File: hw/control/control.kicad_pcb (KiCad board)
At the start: 2 copper layers, 160 x 90 mm, 144 parts, among them J101 Screw_Terminal_01x02, J102 Screw_Terminal_01x03, J103 Screw_Terminal_01x03, J301 Conn_02x05_Odd_Even, J302 Conn_01x04, J303 Raspberry_Pi_0_2_3, J304 Micro_SD_Card, J305 Conn_01x06, J306 Conn_01x07, Q1001 BC807, Q1002 BC817, Q401 BC817, Q501 BC817, Q601 BC817, Q701 BC817, Q801 BC807, Q802 BC817, Q901 AOSP21357, Q902 IRF4905, U1001 LM2678T-ADJ, U1101 SN74AHCT125D, U201 LM2596T-ADJ, U801 LM2678T-ADJ

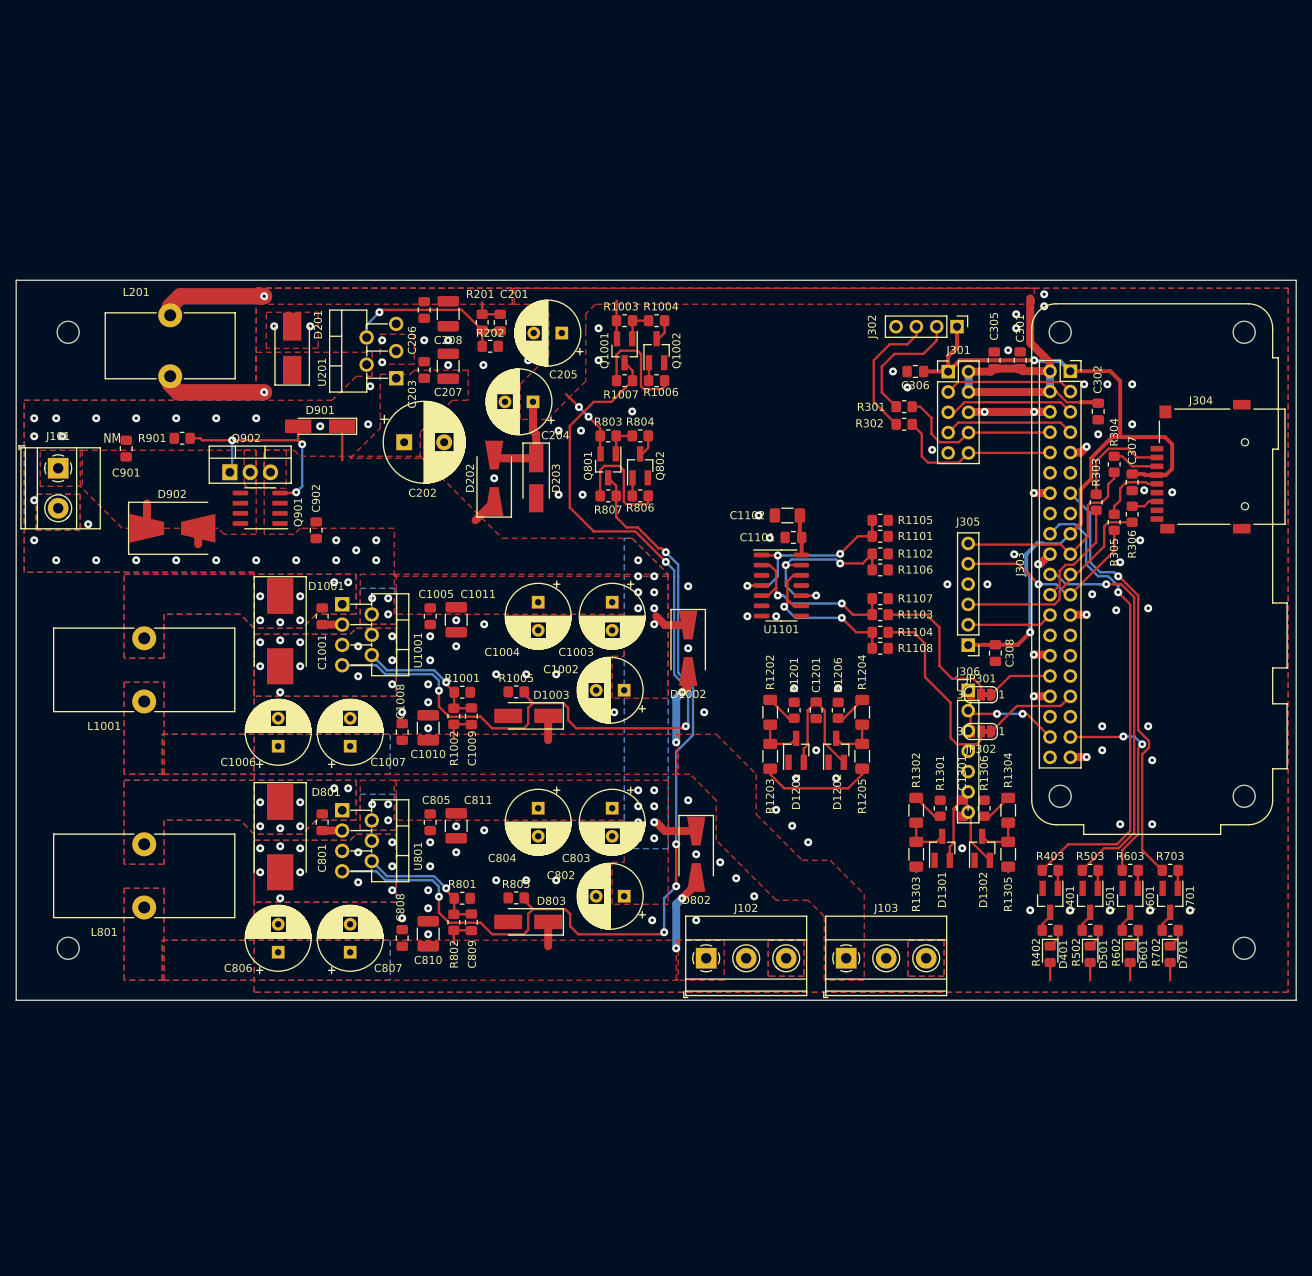
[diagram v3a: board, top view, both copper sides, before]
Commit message: [hw] Lay-out IIS module connector, pwr. enable
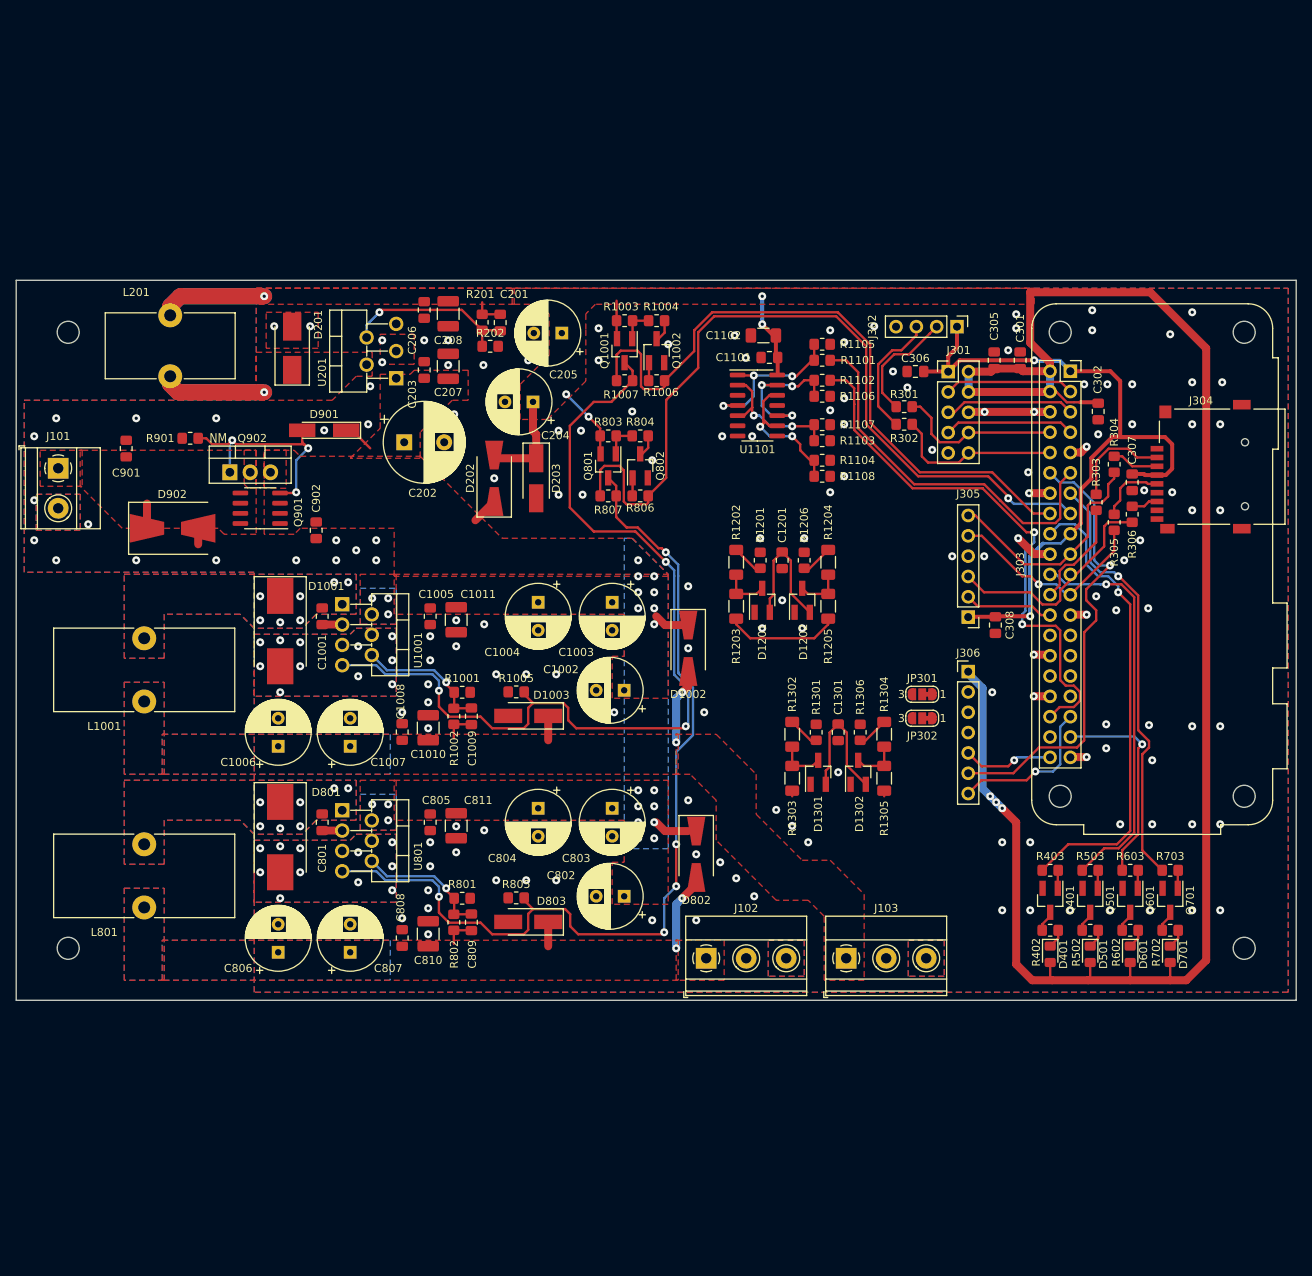
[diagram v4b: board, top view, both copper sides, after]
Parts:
- moved R1101 23.2 mm to (160.8, 60.0)
- moved R1105 23.2 mm to (160.8, 58.0)
- moved R1103 22.9 mm to (160.8, 70.0)
- moved R1107 22.9 mm to (160.8, 68.0)
- moved R1102 22.9 mm to (160.8, 62.5)
- moved R1106 22.9 mm to (160.8, 64.5)
- moved C1101 22.7 mm to (154.2, 59.6)
- moved C1102 22.7 mm to (153.4, 56.9)
- moved U1101 22.7 mm to (152.7, 65.7)
- moved R1104 22.7 mm to (160.8, 72.5)
- moved R1108 22.7 mm to (160.8, 74.5)
- moved C1201 19.2 mm to (155.8, 85.0)
- moved D1201 19.2 mm to (153.2, 90.0)
- moved D1202 19.2 mm to (158.2, 90.0)
- moved R1201 19.2 mm to (153.0, 85.0)
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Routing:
- net +5V: track 148.5 -> 321.3 mm, vias 3 -> 8
- net /LED_PWR_EN0: track 14.7 -> 101.1 mm, vias 0 -> 1
- net /LED_PWR_EN1: track 14.6 -> 84.0 mm
- net /LED_DATA_~EN~1: track 0.00 -> 68.6 mm, vias 0 -> 2
- net /CPU/IIS_BCLK: track 0.00 -> 56.9 mm, vias 0 -> 1
- net /LED_DATA_~EN~0: track 0.00 -> 47.7 mm
- net /LED_DATA1: track 23.7 -> 0.00 mm
- net /CPU/IIS_LRC: track 0.00 -> 19.5 mm, vias 0 -> 1
- net /LED_DATA0: track 19.2 -> 0.00 mm
- net /CPU/ALT_LED_DATA: track 15.8 -> 0.00 mm, vias 2 -> 0
- net Net-(J303-Pad33): track 11.7 -> 0.00 mm
- net /CPU/IIS_DIN: track 0.00 -> 11.4 mm, vias 0 -> 1
- net Net-(J303-Pad32): track 8.30 -> 0.00 mm
- net Net-(R1102-Pad1): track 24.5 -> 19.6 mm
- net Net-(R1103-Pad2): track 22.3 -> 17.7 mm
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
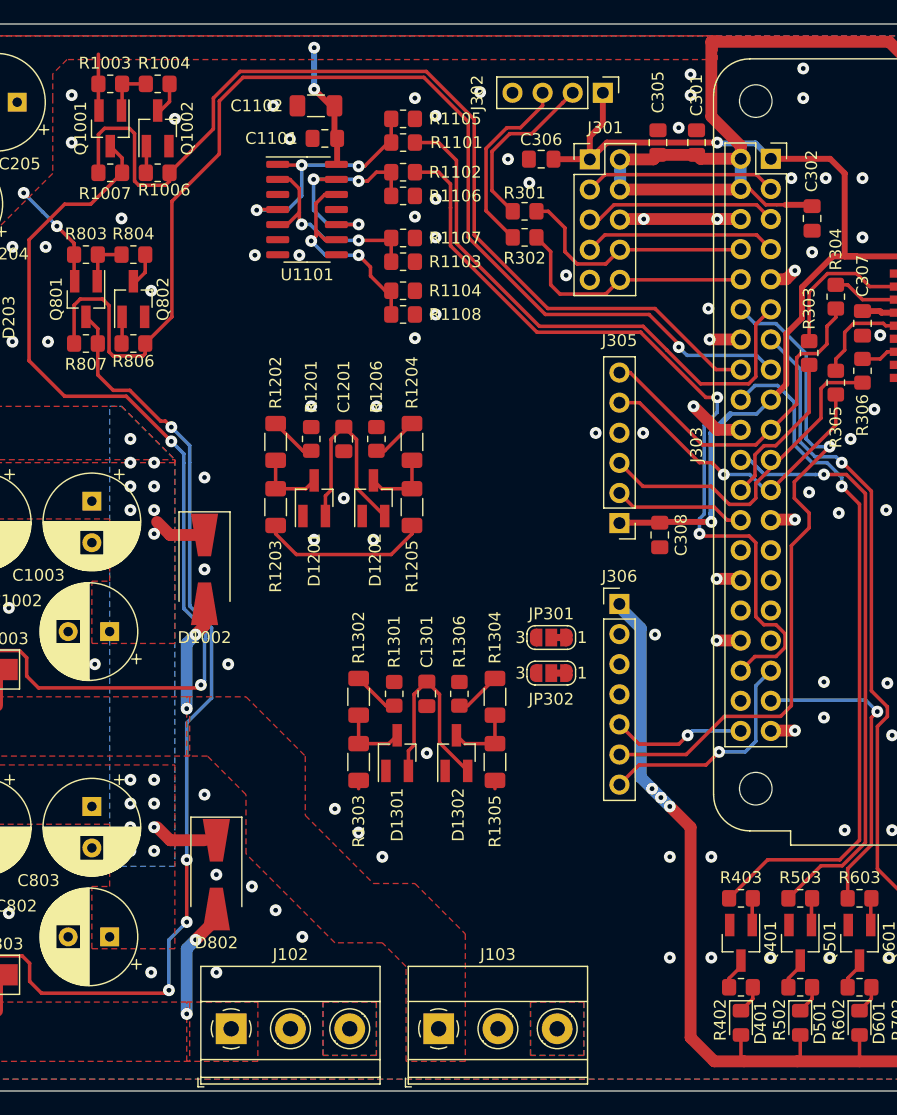
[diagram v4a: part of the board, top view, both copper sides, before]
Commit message: [hw] Length-match IIS and SPI module signals
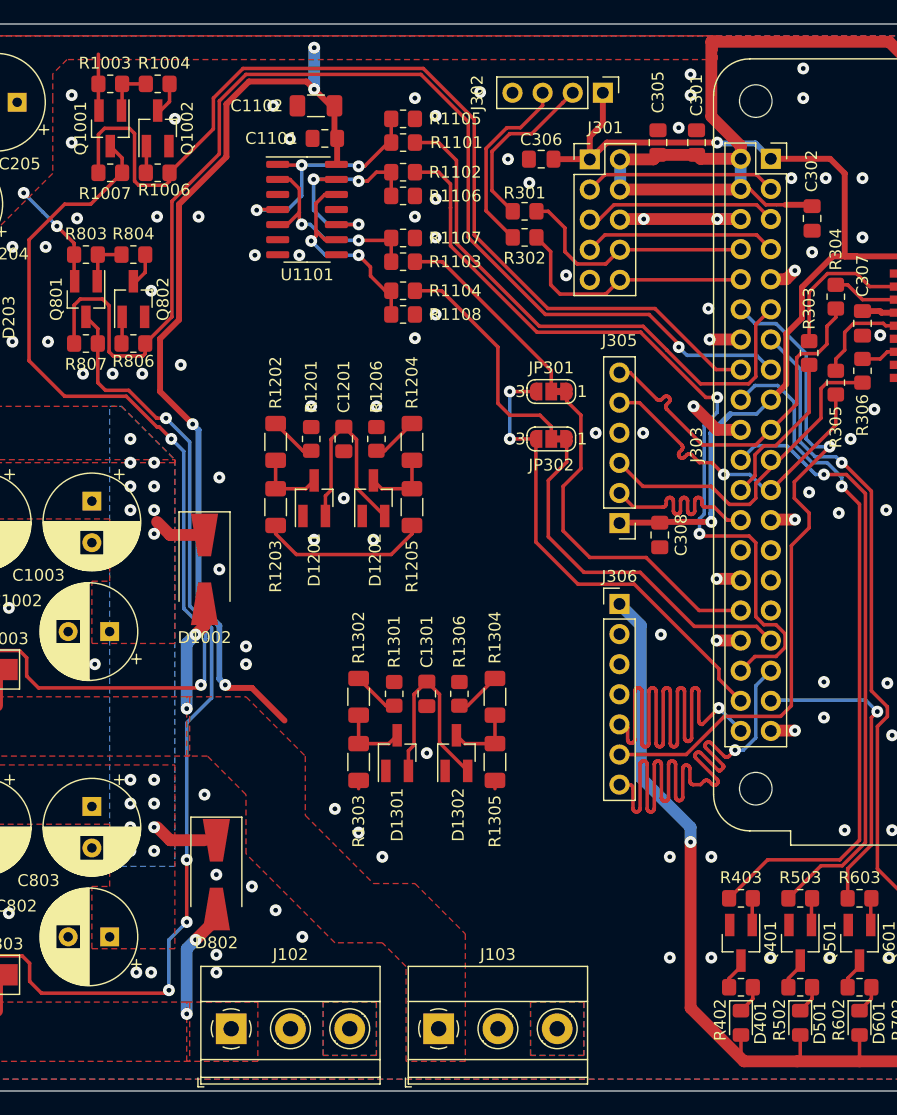
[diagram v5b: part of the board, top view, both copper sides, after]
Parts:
- moved JP301 20.8 mm to (173.2, 81.0)
- moved JP302 19.8 mm to (173.2, 85.0)
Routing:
- net +5V: track 321.3 -> 388.5 mm
- net /CPU/IIS_DIN: track 11.4 -> 57.0 mm
- net /CPU/ALT_LED_DATA: track 0.00 -> 40.4 mm, vias 0 -> 2
- net /CPU/IIS_LRC: track 19.5 -> 57.0 mm
- net Net-(J303-Pad33): track 0.00 -> 31.3 mm
- net Net-(J303-Pad32): track 0.00 -> 30.6 mm
- net /LED_DATA1: track 0.00 -> 20.1 mm
- net /LED_DATA0: track 0.00 -> 17.1 mm
- net /CPU/SPI0_CS1: track 11.2 -> 17.0 mm
- net /CPU/SPI0_CLK: track 26.2 -> 27.3 mm
- net /CPU/SPI0_MOSI: track 29.1 -> 30.3 mm
- net /CPU/Status LED 1/IN_3V3: track 49.6 -> 50.6 mm
- net /LED0 Power/ENABLE: track 115.8 -> 116.3 mm
- net GND: vias 178 -> 188

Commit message: [hw] Complete control layout
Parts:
- moved R1203 37.8 mm to (168.5, 123.7)
- moved R1205 34.4 mm to (171.2, 123.7)
- moved C1102 23.9 mm to (148.2, 80.2), turned to 270 degrees
- moved C1201 23.3 mm to (159.2, 108.0), turned to 90 degrees
- moved D1201 23.1 mm to (157.2, 112.8), turned to 270 degrees
- moved R1202 23.0 mm to (156.8, 107.2)
- moved D1202 22.9 mm to (161.2, 112.8), turned to 270 degrees
- moved R1204 22.0 mm to (161.8, 107.2)
- moved R1303 21.1 mm to (174.8, 123.7)
- moved R1101 19.1 mm to (162.2, 79.0)
- moved R1102 19.1 mm to (162.2, 81.5)
- moved R1103 19.1 mm to (162.2, 89.0)
- moved R1104 19.1 mm to (162.2, 91.5)
- moved R1105 19.1 mm to (162.2, 77.0)
- moved R1106 19.1 mm to (162.2, 83.5)
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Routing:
- net /LED Driver/LED Driver Output 1/IN_B: track 3.95 -> 38.5 mm, vias 0 -> 2
- net /LED Driver/LED Driver Output 0/IN_B: track 3.95 -> 30.7 mm
- net /LED Driver/LED Driver Output 0/IN_A: track 3.95 -> 29.2 mm
- net /LED Driver/LED Driver Output 1/IN_A: track 3.95 -> 27.6 mm
- net /LED Driver/DATA_OUT0: track 14.3 -> 34.2 mm
- net +5V: track 388.5 -> 407.0 mm, vias 8 -> 10
- net Net-(D1201-Pad3): track 5.94 -> 20.9 mm
- net Net-(D1202-Pad3): track 5.94 -> 20.2 mm
- net /LED Driver/DATA_OUT1: track 1.40 -> 15.5 mm
- net /LED_DATA_~EN~0: track 47.7 -> 37.2 mm
- net Net-(D1301-Pad3): track 5.94 -> 16.0 mm
- net Net-(D1302-Pad3): track 5.94 -> 15.6 mm
- net Net-(J303-Pad32): track 30.6 -> 21.7 mm
- net /LED_DATA1: track 20.1 -> 11.3 mm
- net Net-(J303-Pad33): track 31.3 -> 22.9 mm
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
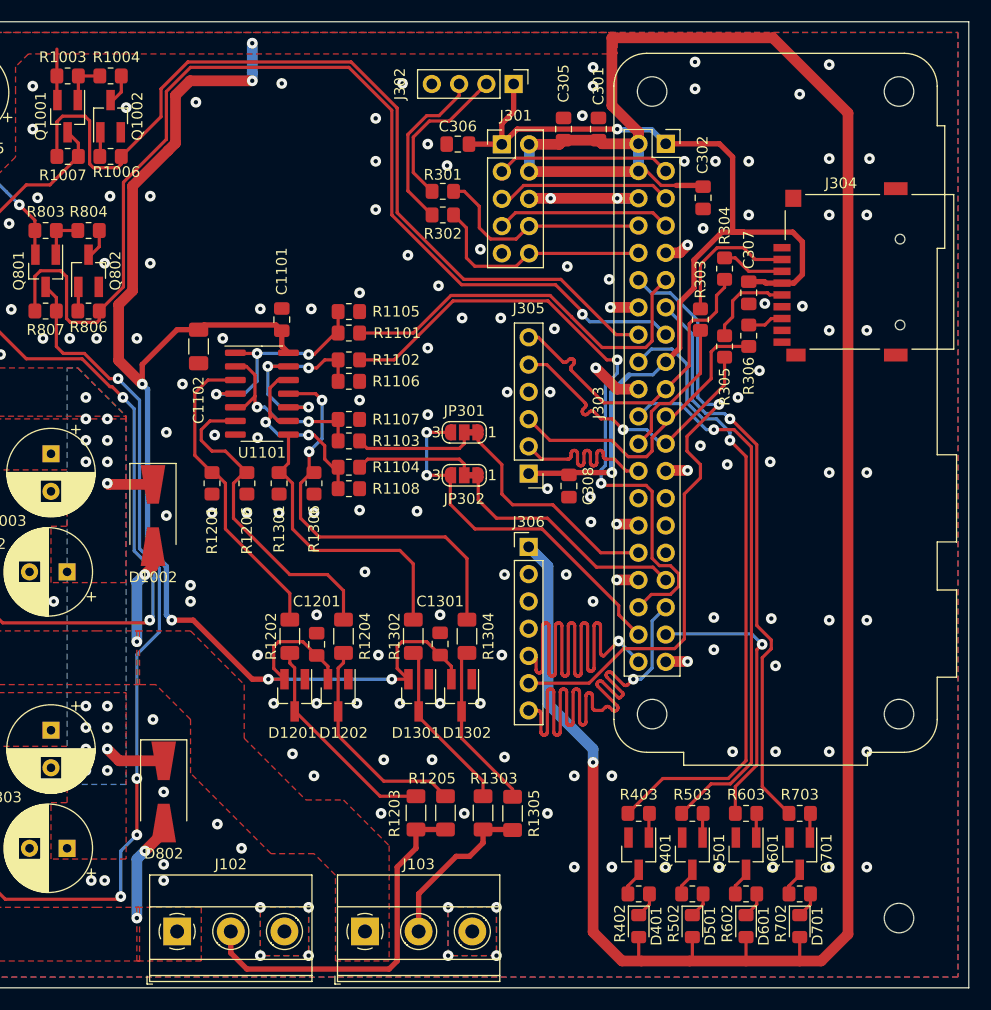
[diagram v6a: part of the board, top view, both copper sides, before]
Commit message: [hw] Add button, move sd card
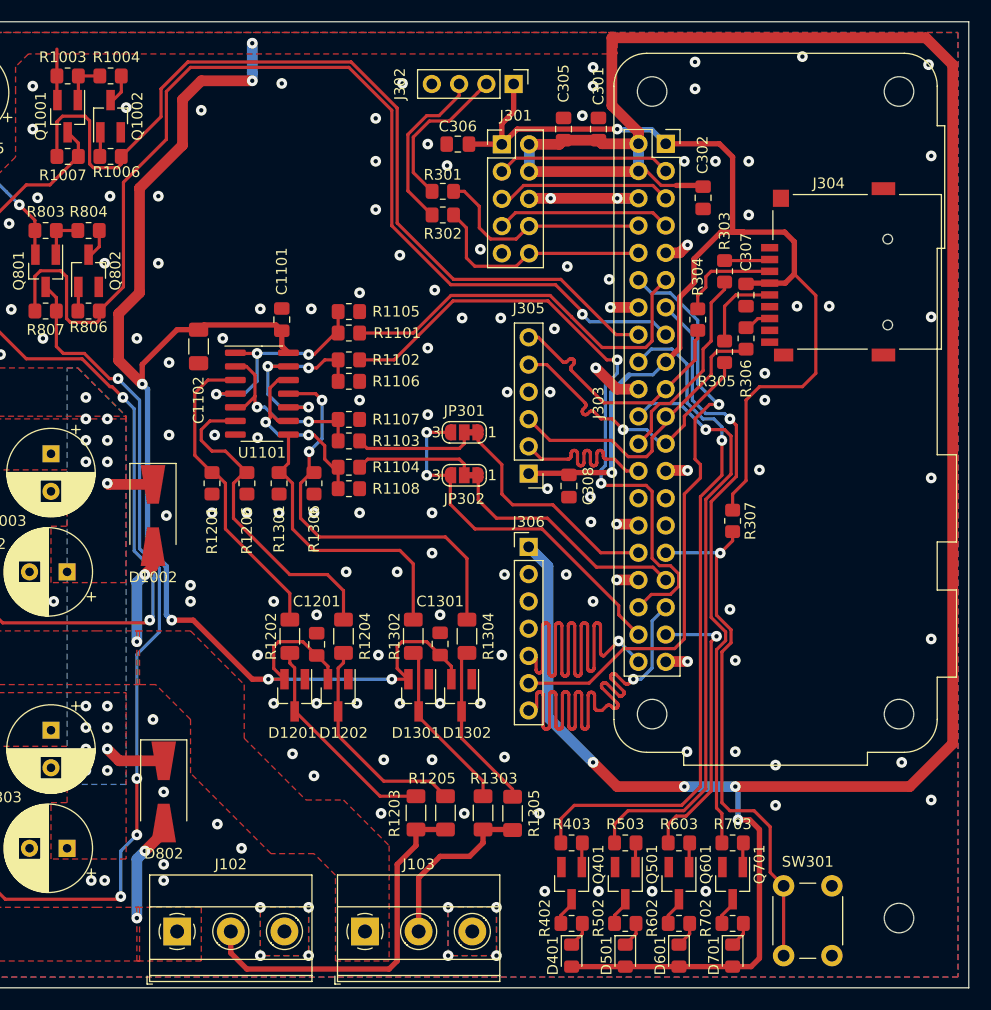
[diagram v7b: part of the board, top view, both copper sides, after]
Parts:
- added R307: 10K, Resistor_SMD:R_0805_2012Metric_Pad1.20x1.40mm_HandSolder, F.Cu at (198.0, 96.5)
- added SW301: SW_Push, Button_Switch_THT:SW_PUSH_6mm, F.Cu at (202.8, 137.0)
- moved D401 6.83 mm to (183.0, 137.0)
- moved D501 6.83 mm to (188.0, 137.0)
- moved D601 6.83 mm to (193.0, 137.0)
- moved D701 6.83 mm to (198.0, 137.0)
- moved Q401 6.83 mm to (183.0, 130.2)
- moved Q501 6.83 mm to (188.0, 130.2)
- moved Q601 6.83 mm to (193.0, 130.2)
- moved Q701 6.83 mm to (198.0, 130.2)
- moved R402 6.83 mm to (183.0, 134.0)
- moved R403 6.83 mm to (183.0, 126.5)
- moved R502 6.83 mm to (188.0, 134.0)
- moved R503 6.83 mm to (188.0, 126.5)
- moved R602 6.83 mm to (193.0, 134.0)
- moved R603 6.83 mm to (193.0, 126.5)
- moved R702 6.83 mm to (198.0, 134.0)
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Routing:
- net Net-(J303-Pad31): track 0.00 -> 49.8 mm, vias 0 -> 1
- net +3V3: track 93.2 -> 120.3 mm
- net +5V: track 407.0 -> 421.7 mm, vias 10 -> 13
- net Net-(J304-Pad2): track 12.8 -> 4.49 mm
- net /CPU/SPI0_MOSI: track 30.3 -> 23.7 mm
- net /CPU/Status LED 0/IN_3V3: track 58.6 -> 64.2 mm
- net /CPU/SPI0_CS0: track 13.5 -> 19.0 mm
- net /CPU/Status LED 1/IN_3V3: track 50.6 -> 55.8 mm
- net Net-(J304-Pad3): track 5.87 -> 9.47 mm
- net /CPU/Status LED 3/IN_3V3: track 53.7 -> 55.7 mm
- net /LED Driver/DATA_OUT1: track 15.5 -> 16.4 mm
- net /CPU/SPI0_MISO: track 28.8 -> 27.9 mm
- net /CPU/IIS_BCLK: track 56.9 -> 56.1 mm
- net Net-(J304-Pad7): track 3.35 -> 2.55 mm
- net /CPU/IIS_LRC: track 57.0 -> 56.2 mm
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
